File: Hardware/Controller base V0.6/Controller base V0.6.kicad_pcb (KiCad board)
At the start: 2 copper layers, 30 x 50 mm, 27 parts, among them J1 USB_C_Receptacle_USB2.0_16P, J7 Conn_02x10_Counter_Clockwise, J8 Conn_02x10_Counter_Clockwise, SW4 SW_Push, U1 AZ1117CH-3.3TRG1, U2 ESP32-S3-WROOM-1U-N4

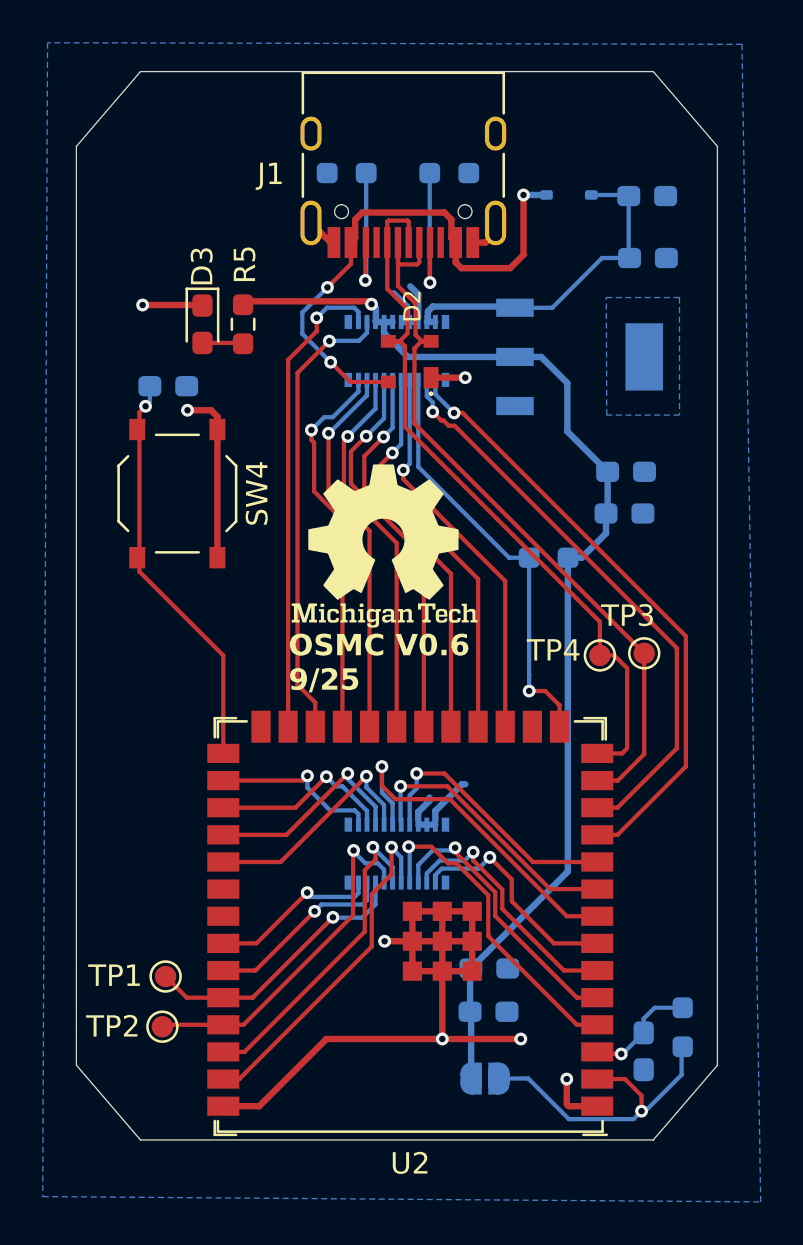
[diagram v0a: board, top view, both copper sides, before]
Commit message: centered components
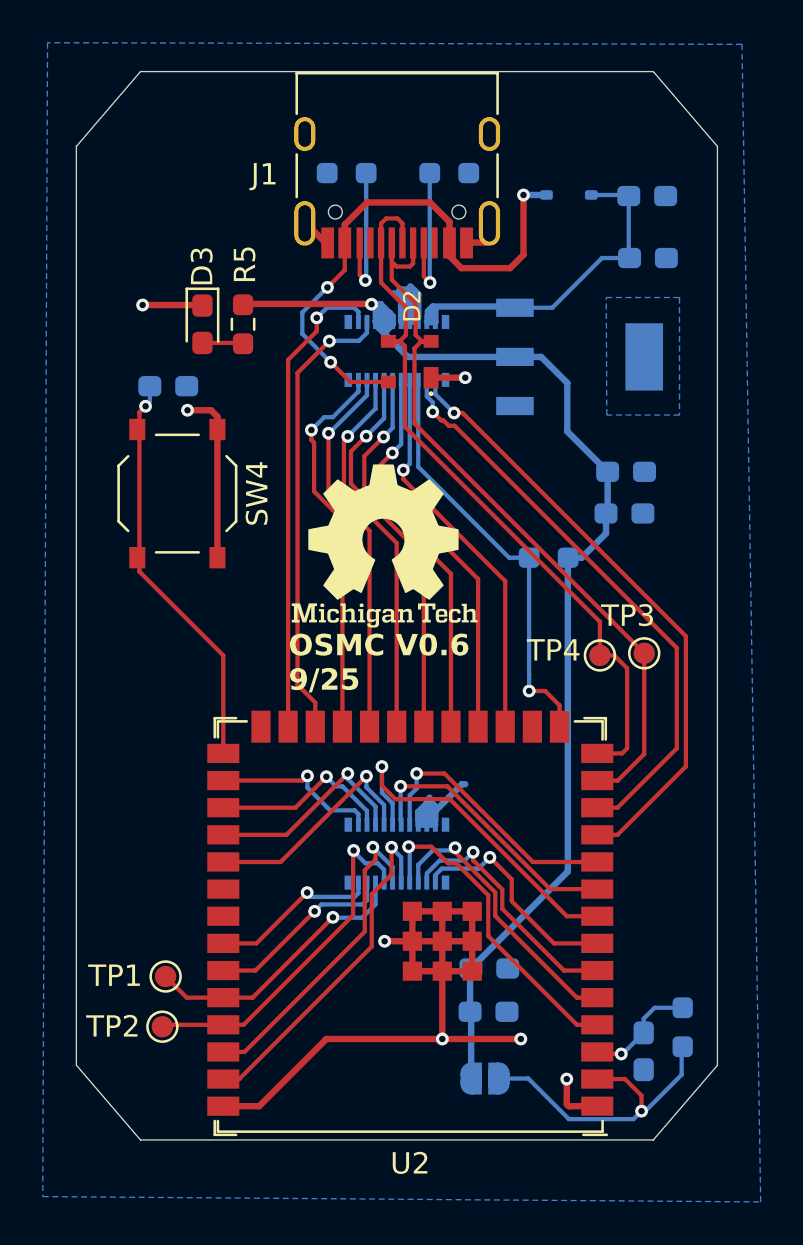
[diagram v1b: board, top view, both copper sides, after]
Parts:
- moved J1 0.29 mm to (143.0, 72.9)
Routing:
- net GND: track 63.3 -> 72.9 mm
- net VCC_3V3: track 54.4 -> 61.1 mm
- net VCC_5V: track 15.9 -> 17.2 mm
- net D-: track 35.5 -> 34.8 mm

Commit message: update
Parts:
- added H1: MountingHole, MountingHole:MountingHole_2.5mm, F.Cu at (153.9, 73.2)
- added H2: MountingHole, MountingHole:MountingHole_2.5mm, F.Cu at (131.9, 73.2)
- moved D1 1.88 mm to (151.0, 76.5)
- moved C1 1.85 mm to (154.7, 76.6)
- moved C6 1.67 mm to (153.7, 91.2)
- moved U1 1.60 mm to (151.6, 83.9)
- moved R3 1.47 mm to (150.1, 93.1)
- moved C4 1.45 mm to (153.7, 89.1)
- moved C2 1.40 mm to (154.7, 79.0)
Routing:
- net GND: track 72.9 -> 75.4 mm
- net VBUS: track 26.0 -> 24.1 mm
- net VCC_5V: track 17.2 -> 17.9 mm
- net GPIO3: track 19.8 -> 19.2 mm

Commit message: slimed down files
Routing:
- net unconnected-(U1-EPAD-Pad4): vias 0 -> 4
- added copper zone on F.Cu, net unconnected-(U1-EPAD-Pad4)
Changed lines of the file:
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@@
 		(net 42)
+	)
+	(via
+		(at 156.3 86.175)
+		(size 0.6)
+		(drill 0.3)
+		(layers "F.Cu" "B.Cu")
+		(free yes)
+		(net 43)
+	)
+	(via
+		(at 156.3 81.525)
+		(size 0.6)
+		(drill 0.3)
+		(layers "F.Cu" "B.Cu")
+		(free yes)
+		(net 43)
+	)
+	(via
+		(at 153.225 81.5)
+		(size 0.6)
+		(drill 0.3)
+		(layers "F.Cu" "B.Cu")
+		(free yes)
+		(net 43)
+	)
+	(via
+		(at 153.3 86.175)
+		(size 0.6)
+		(drill 0.3)
+		(layers "F.Cu" "B.Cu")
+		(free yes)
+		(net 43)
 	)
 	(segment
@@
 	)
 	(zone
+		(net 43)
+		(net_name "unconnected-(U1-EPAD-Pad4)")
+		(layer "F.Cu")
+		(hatch edge 0.5)
+		(priority 2)
+		(connect_pads
+			(clearance 0)
+		)
+		(min_thickness 0.25)
+		(filled_areas_thickness no)
+		(fill yes
+			(thermal_gap 0.5)
+			(thermal_bridge_width 0.5)
+		)
+		(polygon
+			(pts
+				(xy 151.65 80.425) (xy 151.65 87.525) (xy 157.65 87.525) (xy 157.675 80.425)
+			)
+		)
+	)
+	(zone
 		(net 1)
 		(net_name "GND")
@@
 		(polygon
 			(pts
-				(xy 152.825 81.075) (xy 156.252736 81.075) (xy 156.252736 86.575) (xy 152.85 86.575)
+				(xy 152.842044 81.075) (xy 156.752736 81.075) (xy 156.752736 86.575) (xy 152.867044 86.575)
 			)
 		)
